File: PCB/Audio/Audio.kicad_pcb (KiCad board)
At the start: 2 copper layers, 70 x 70 mm, 42 parts, among them J1 Battery, J3 TC2030-USB-NL-DS, J4 TF_PUSH, J5 USB-C-Socket-H, Q2 CJ2301, SW1 SW_Push, U1 R, U2 L, U3 TP4054, U4 ME6211C33M5G-N, U6 ESP32-S3-MINI-1

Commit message: New layout
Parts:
- added C10: 100nF, RevK:C_0402, F.Cu at (119.5, 92.9)
- added C5: 100nF, RevK:C_0402, B.Cu at (91.0, 108.0)
- added D6: XL-1010RGBC-WS2812B, RevK:SMD1010, F.Cu at (121.1, 91.8)
- added J2: Reset, RevK:AA-Pad, F.Cu at (84.8, 93.9)
- added R3: 10K, RevK:R_0402, F.Cu at (98.3, 108.8)
- C7, J1, R10, R11, R12, R13, R9: moved to F.Cu
- D4: value ~ -> XL-1010RGBC-WS2812B; footprint RevK:DFN1006-2L -> RevK:SMD1010
- moved R13 10.9 mm to (94.0, 108.8), turned to 90 degrees
- moved R12 10.3 mm to (94.9, 108.8), turned to 90 degrees
- moved R11 9.82 mm to (95.8, 108.8), turned to 90 degrees
- moved R2 9.77 mm to (108.7, 94.4)
- moved J1 9.64 mm to (116.8, 105.1), turned to 180 degrees
- moved R10 9.49 mm to (96.6, 108.8), turned to 90 degrees
- moved C4 9.45 mm to (108.7, 107.2), turned to 180 degrees
- moved R9 9.31 mm to (97.5, 108.8), turned to 90 degrees
- moved D5 8.94 mm to (90.0, 108.0), turned to 180 degrees
- moved D1 8.89 mm to (111.0, 107.3), turned to -135 degrees
- moved C9 8.49 mm to (108.6, 95.9), turned to -90 degrees
- moved R6 6.05 mm to (122.0, 107.0), turned to -90 degrees
- moved R5 5.49 mm to (122.0, 105.0)
- moved C6 5.40 mm to (91.0, 92.0), turned to 90 degrees
- moved D3 4.26 mm to (117.2, 91.4), turned to 0 degrees
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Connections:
- D1 pad 1: unconnected-(D1-O-Pad1) -> Net-(D1-O)
- D4 pad 1: BUTTON -> unconnected-(D4-O-Pad1)
- D4 pad 2: GND -> +3V3
- D5 pad 1: unconnected-(D5-O-Pad1)_1 -> Net-(D4-I)
- J1 pad 1: GND -> VBAT
- J1 pad 2: VBAT -> GND
- J4 pad 8: Net-(J4-DAT1) -> SDDAT1
- R9 pad 2: Net-(J4-DAT1) -> SDDAT1
- U6 pad 12: GND -> unconnected-(U6-GPIO8-Pad12)
- U6 pad 15: GND -> unconnected-(U6-GPIO11-Pad15)
- U6 pad 18: unconnected-(U6-GPIO14-Pad18) -> SDSCK
- U6 pad 19: SDSCK -> SDMISO
- U6 pad 20: SDMISO -> SDDAT1
- U6 pad 25: unconnected-(U6-GPIO21-Pad25) -> Net-(J2-Pin_2)
- U6 pad 40: CHARGING -> unconnected-(U6-GPIO44-Pad40)
- U6 pad 6: GND -> unconnected-(U6-GPIO2-Pad6)
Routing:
- net Net-(D1-O): track 0.00 -> 30.9 mm, vias 0 -> 2
- net Net-(J4-DAT1): track 29.0 -> 0.00 mm
- net Net-(D4-I): track 0.00 -> 23.9 mm, vias 0 -> 2
- net SDDAT1: track 0.00 -> 23.7 mm, vias 0 -> 1
- net Net-(J2-Pin_2): track 0.00 -> 22.9 mm, vias 0 -> 2
- net GND: track 72.4 -> 54.6 mm, vias 23 -> 15
- net SCK: track 30.2 -> 19.0 mm, vias 2 -> 1
- net BLINK: track 14.7 -> 3.96 mm, vias 2 -> 0
- net Net-(U6-EN): track 12.8 -> 2.60 mm, vias 2 -> 0
- net D+: track 36.8 -> 28.4 mm
- net SDMISO: track 31.3 -> 23.3 mm
- net SDCD: track 17.4 -> 25.0 mm
- net SDSCK: track 27.4 -> 21.0 mm
- net SDMOSI: track 24.9 -> 19.1 mm
- net Net-(D3-K): track 11.8 -> 6.38 mm
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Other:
- board text added: "1"
- board text added: "12 13 15 16 17 6 7 10"
- board text added: "18"
- board text added: "21"
- board text added: "44"
- board text added: "9"
- board text added: "A"
- board text added: "Audio Recorder"
- board text added: "BTN"
- board text added: "CHG"
- board text added: "LED"
- board text added: "Made in China"
- board text added: "SS MOSI SCK MISO CD WS SD SCK"
- board text removed: "Audio"

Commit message: Correct SS
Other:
- board text added: "12 13 14 15 17 6 7 10"
- board text added: "35"
- board text removed: "12 13 15 16 17 6 7 10"
- board text removed: "44"

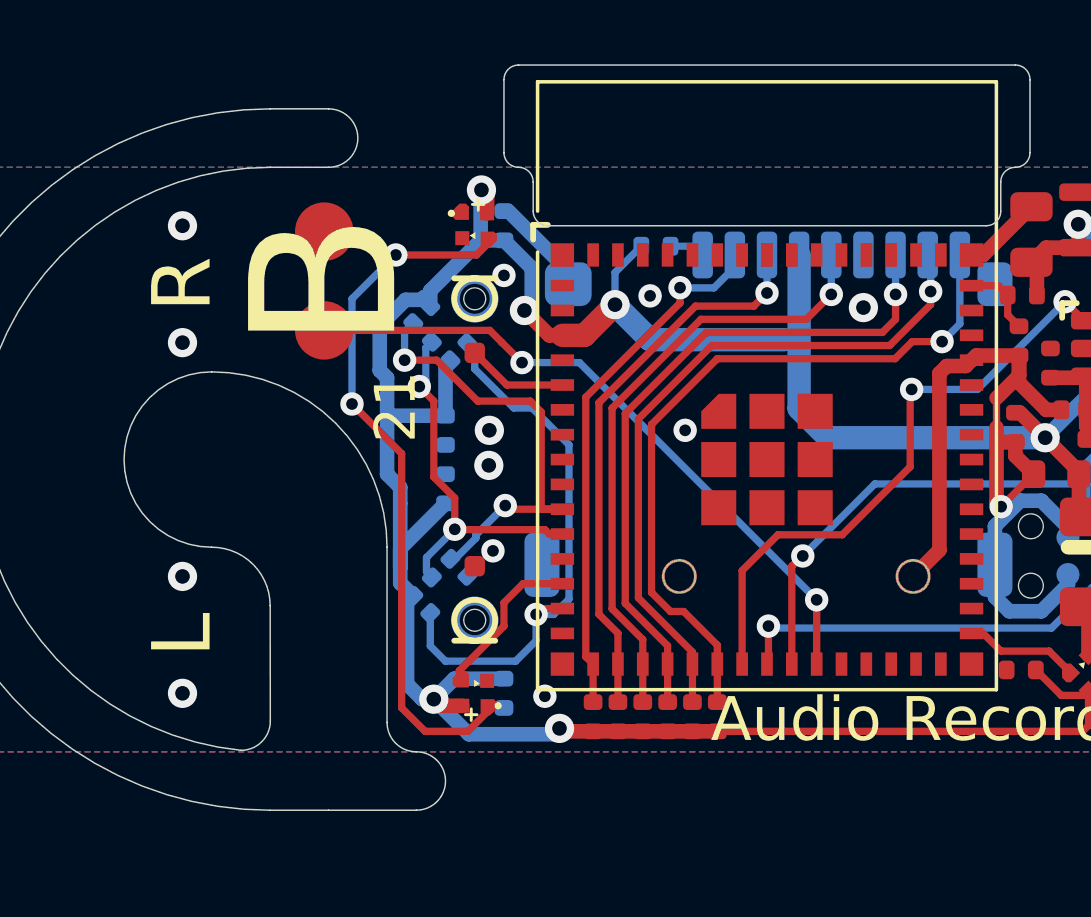
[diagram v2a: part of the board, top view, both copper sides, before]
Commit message: Moved LEDs
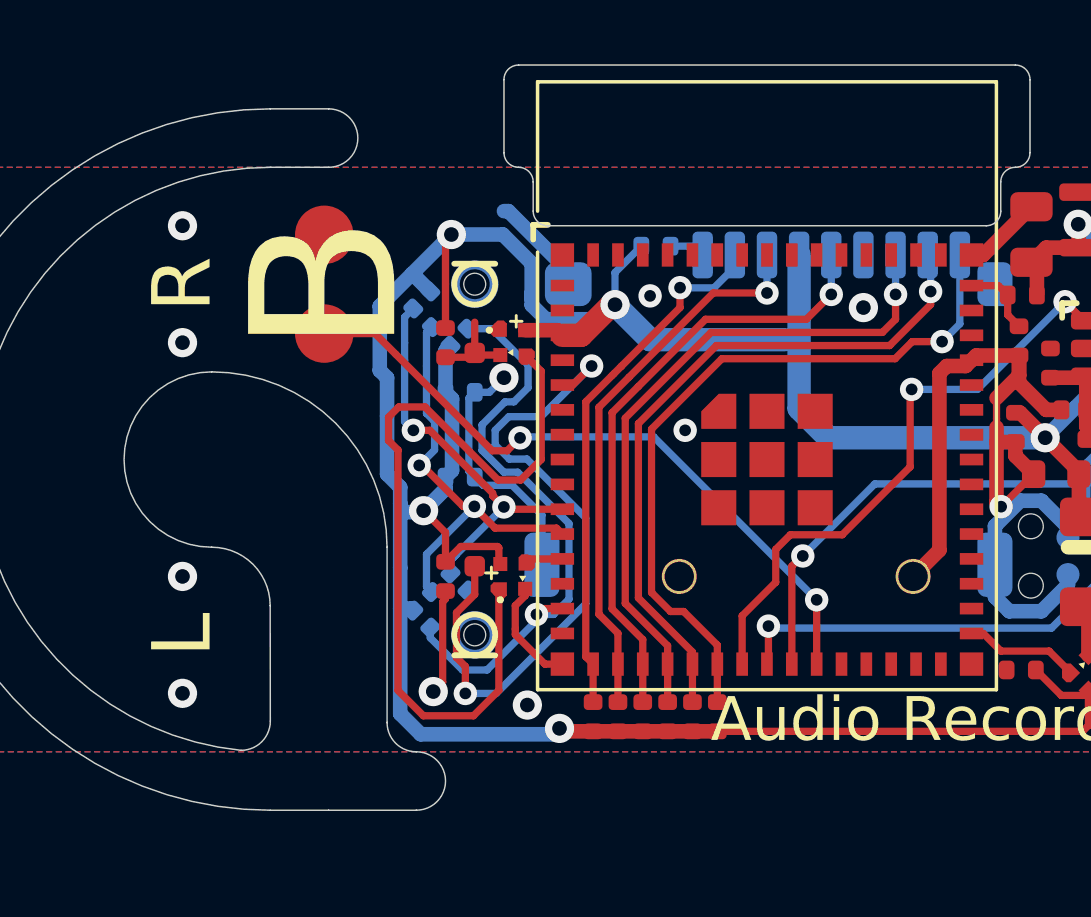
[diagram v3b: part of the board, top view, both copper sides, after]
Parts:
- C5, C6: moved to F.Cu
- moved C5 4.47 mm to (89.0, 104.0)
- moved C6 4.47 mm to (89.0, 96.0), turned to -90 degrees
- moved D4 4.21 mm to (91.3, 96.0)
- moved D5 4.21 mm to (91.3, 104.0), turned to 90 degrees
- moved C8 1.39 mm to (89.5, 97.7), turned to 180 degrees
- moved C13 0.64 mm to (89.5, 100.6), turned to 180 degrees
- moved U1 0.50 mm to (89.4, 94.6)
- moved U2 0.50 mm to (89.4, 105.4)
- moved J2 0.11 mm to (84.8, 94.0)
- turned SW1 to -90 degrees
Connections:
- U6 pad 12: unconnected-(U6-GPIO8-Pad12) -> BLINK2
- U6 pad 13: BLINK2 -> unconnected-(U6-GPIO9-Pad13)
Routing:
- net BUTTON: track 3.46 -> 23.2 mm, vias 0 -> 2
- net GND: track 54.6 -> 73.8 mm, vias 15 -> 13
- net +3V3: track 120.8 -> 127.5 mm, vias 8 -> 7
- net BLINK2: track 5.47 -> 1.25 mm
- net Net-(D4-I): track 23.9 -> 27.5 mm, vias 2 -> 0
- net SD: track 13.0 -> 14.7 mm
- net WS: track 15.5 -> 13.9 mm
- net SCK: track 19.0 -> 20.6 mm

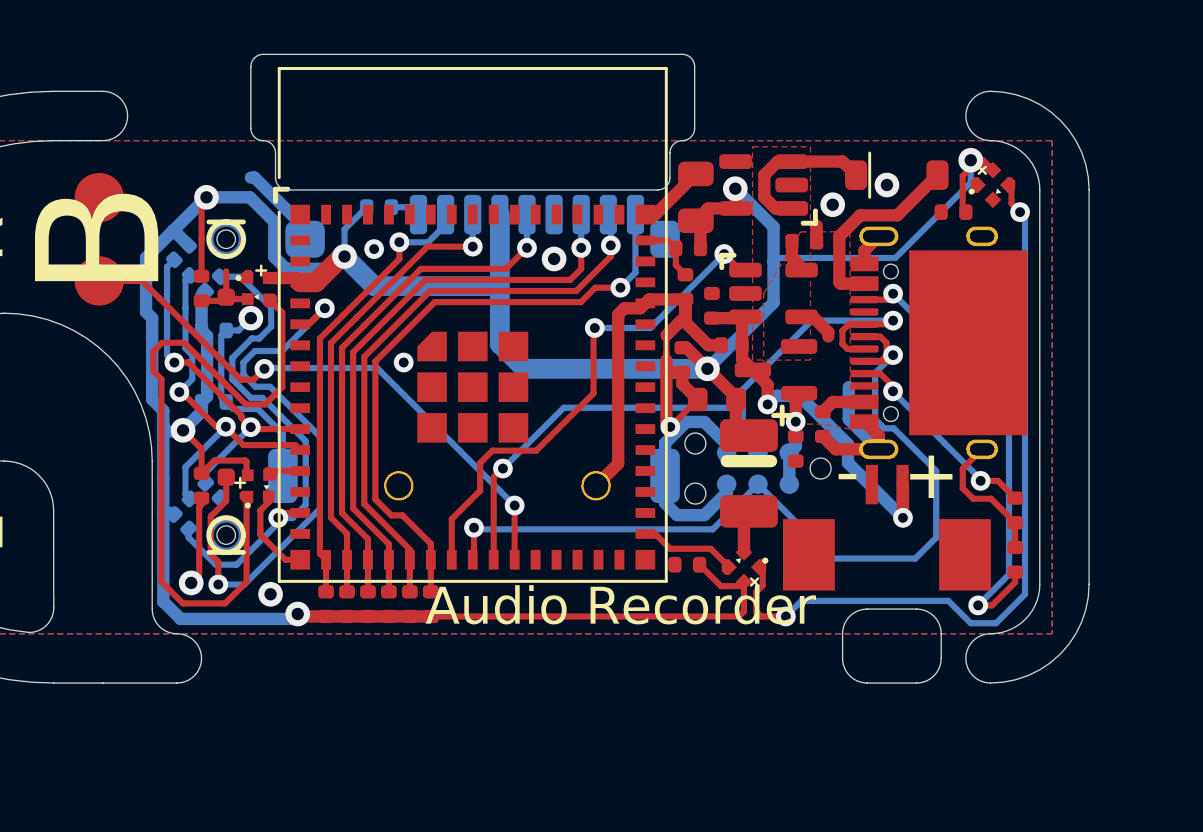
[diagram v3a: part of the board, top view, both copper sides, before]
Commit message: Reworked to have speaker, and VBUS test.
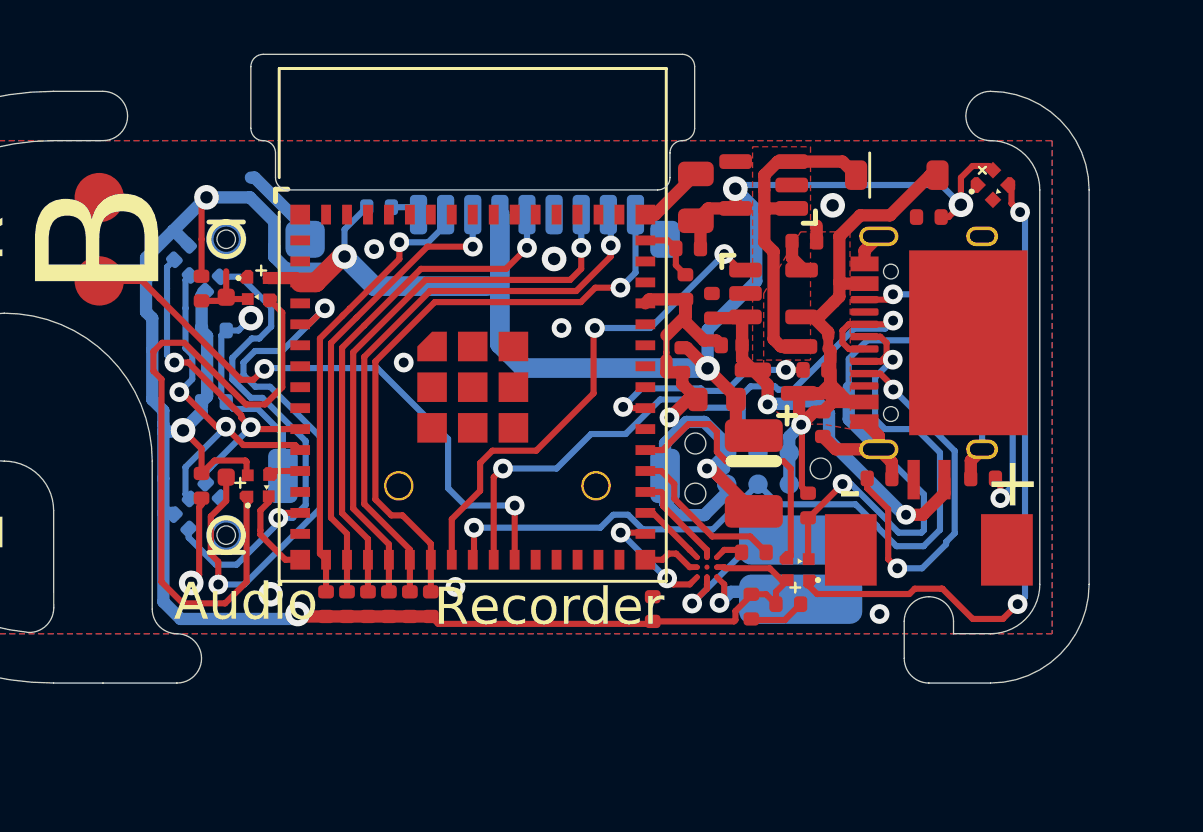
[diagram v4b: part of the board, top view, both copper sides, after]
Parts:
- added C12: 10uF, RevK:C_0402, F.Cu at (111.3, 108.9)
- added C14: 100nF, RevK:C_0402, F.Cu at (112.8, 108.8)
- added R4: 634K, RevK:R_0402, F.Cu at (111.4, 106.7)
- added R7: 10K, RevK:R_0402, F.Cu at (113.9, 99.3)
- added TP1: +, RevK:SolderPadSmall, B.Cu at (113.3, 108.6)
- added TP2: -, RevK:SolderPadSmall, B.Cu at (113.3, 106.2)
- added U5: MAX98357A, RevK:WLP-1.437mmx1.347mm-0.21mm-ball, F.Cu at (109.5, 107.3)
- moved R5 5.65 mm to (116.5, 103.7), turned to 0 degrees
- moved R6 3.55 mm to (120.7, 103.7), turned to 0 degrees
- moved R8 2.35 mm to (113.6, 104.8)
- moved C4 2.28 mm to (107.3, 109.0), turned to 90 degrees
- moved D1 2.20 mm to (113.2, 107.4), turned to 180 degrees
- moved J1 1.71 mm to (118.5, 104.9)
- moved C10 1.02 mm to (118.5, 93.1)
- moved C1 0.20 mm to (111.4, 103.5)
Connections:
- U6 pad 31: BLINK -> SKPWS
- U6 pad 32: unconnected-(U6-GPIO36-Pad32) -> SKPSCK
- U6 pad 33: unconnected-(U6-GPIO37-Pad33) -> SKPSD
- U6 pad 34: unconnected-(U6-GPIO38-Pad34) -> SKPPWR
- U6 pad 35: unconnected-(U6-GPIO39-Pad35) -> BLINK
- U6 pad 37: unconnected-(U6-GPIO41-Pad37) -> Net-(U6-GPIO41)
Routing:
- net GND: track 73.8 -> 89.7 mm, vias 13 -> 17
- net VBUS: track 15.8 -> 29.8 mm
- net Net-(U6-GPIO41): track 0.00 -> 8.92 mm, vias 0 -> 2
- net BLINK: track 3.96 -> 11.4 mm
- net Net-(J5-CC1): track 8.36 -> 15.5 mm
- net Net-(D3-K): track 6.38 -> 13.3 mm
- net SKPPWR: track 0.00 -> 6.62 mm
- net Net-(U5-OUTN): track 0.00 -> 6.49 mm, vias 0 -> 1
- net SKPWS: track 0.00 -> 4.69 mm, vias 0 -> 2
- net Net-(J5-CC2): track 18.7 -> 14.2 mm
- net Net-(U5-OUTP): track 0.00 -> 4.31 mm, vias 0 -> 1
- net Net-(D1-O): track 30.9 -> 27.0 mm
- net SKPSD: track 0.00 -> 3.77 mm
- net SKPSCK: track 0.00 -> 2.42 mm
- net VBAT: track 14.8 -> 16.0 mm
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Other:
- board text added: "37"
- board text added: "39"
- board text added: "8"
- board text added: "Audio"
- board text added: "B"
- board text added: "Recorder"
- board text added: "VBUS"
- board text removed: "35"
- board text removed: "9"
- board text removed: "Audio Recorder"
- board text removed: "BA"
- board text removed: "Made in China"

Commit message: Tidy
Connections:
- U5 pad B2: unconnected-(U5-GAIN_SLOT-PadB2) -> GND
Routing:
- net GND: track 89.7 -> 90.4 mm
